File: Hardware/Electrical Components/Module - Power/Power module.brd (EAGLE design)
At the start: 140 x 70 mm, 97 parts

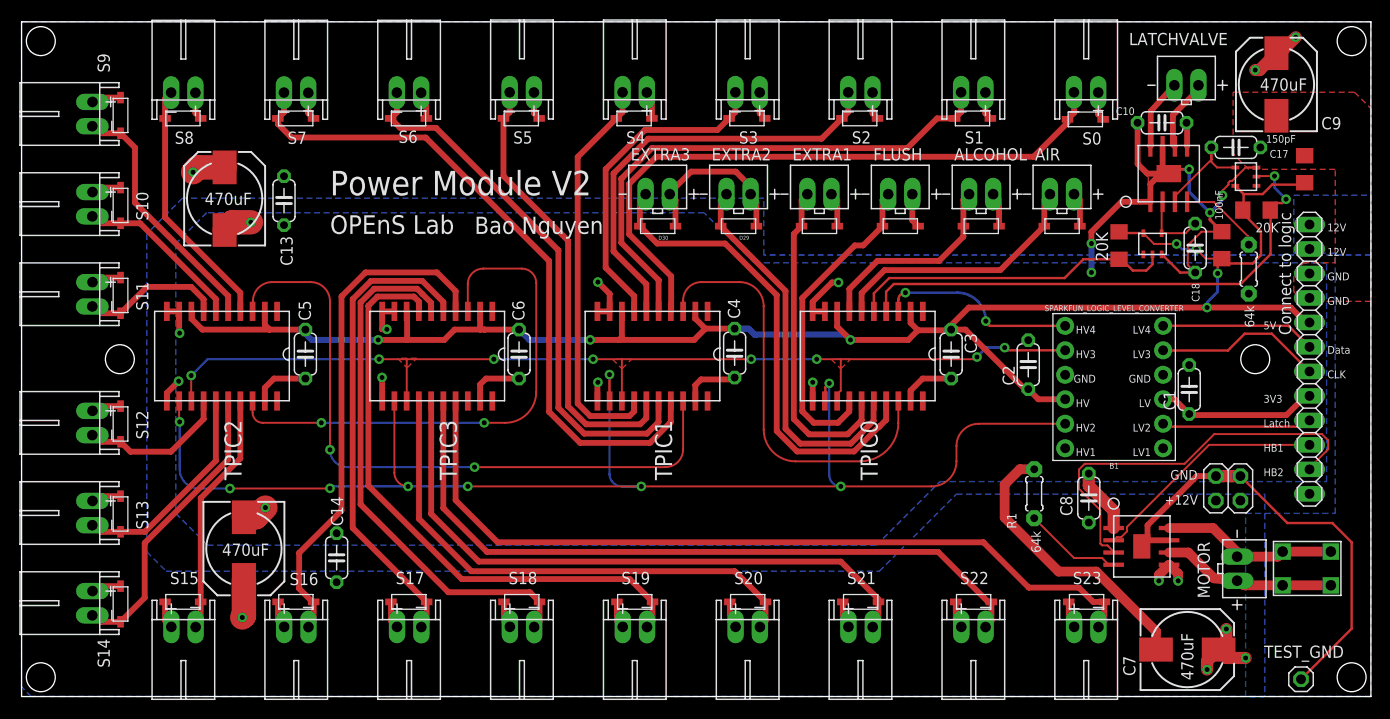
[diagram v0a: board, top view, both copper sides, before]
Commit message: Major fix for sensor module
O Power Module: Changes in footprint location of motor push-to-connect for mounting place. Move the 90-angle header further inside for better mechanical support
O Sensor Module: Rearrange 2.5mm headphone jack closer to the edge for proper mounting. The older version stops the male jack fully dock with the female casing thus fail to connect. Move the 90-angle header further inside for better mechanical support.
O MS5803-02BA: Change symbol, change SDA -> SDO. This label caused the PCB to stop working with all I2C devices. Sensor Module: Rewire to the write SDA, tested.
+ Add MS5803-02BA Datasheet
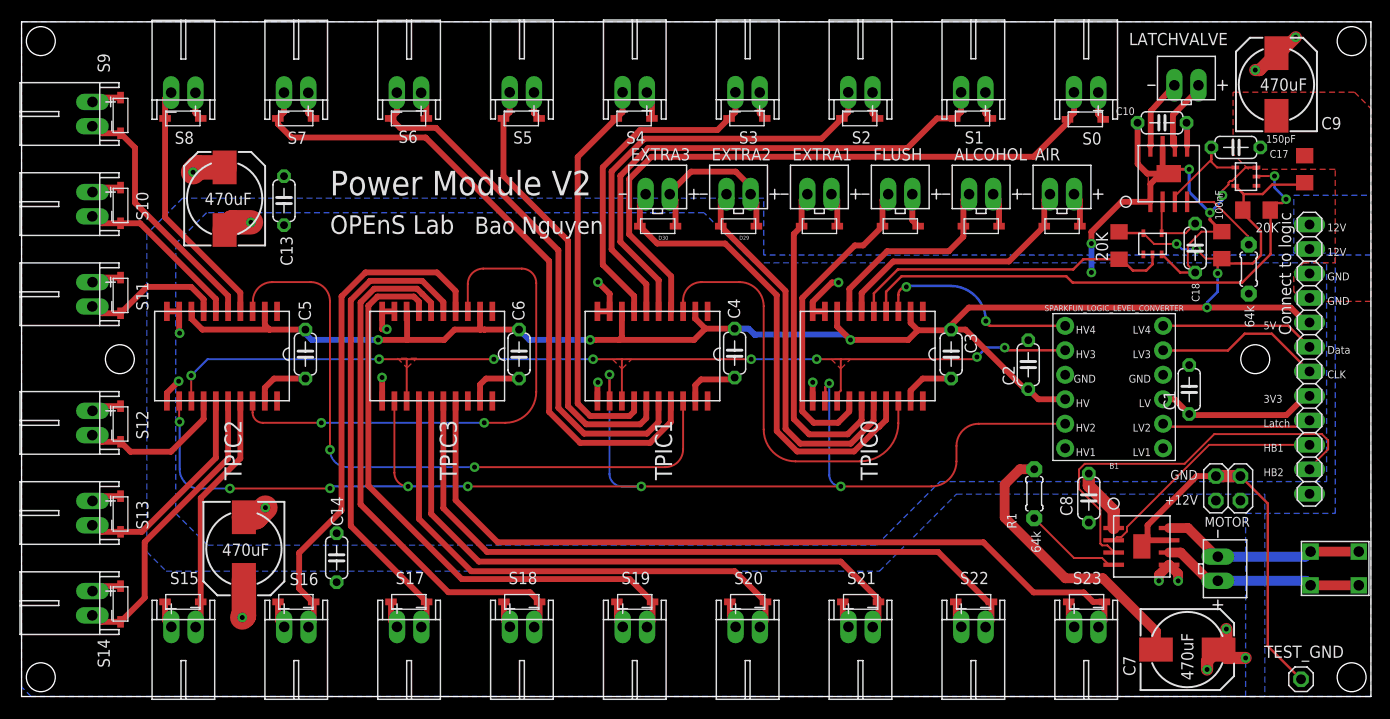
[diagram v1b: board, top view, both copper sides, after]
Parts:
- moved U$1 2.90 mm to (136.1, 13.3)
- moved MOTOR 2.00 mm to (124.1, 13.3)
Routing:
- net GND: track 195.0 -> 187.9 mm
- net MOTOR2: track 18.0 -> 21.1 mm
- net MOTOR1: track 18.5 -> 21.1 mm
- net T_DATA: track 20.2 -> 21.1 mm
- net S4: track 33.9 -> 34.5 mm
- net LATCHVALVE1: track 55.2 -> 55.7 mm
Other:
- board text added: "Designed at Oregon State University"
- board text removed: "Designed and Assembled in Oregon State University"

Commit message: Updates
Updated eDNA Eagle Library
Update OpenSPower7.2 BOM
Add OpenSPower 7.2 ReadMe
Add picture for FlowSensor
General clean up
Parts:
- removed C2: 100nF, adafruit:C050-024X044
- moved U$1 5.00 mm to (131.1, 13.3)
- moved AIR 4.00 mm to (103.9, 52.1)
- moved ALCOHOL 4.00 mm to (95.6, 52.1)
- moved C10 4.00 mm to (114.3, 59.5)
- moved C11 4.00 mm to (120.5, 46.8)
- moved C12 4.00 mm to (129.1, 54.7)
- moved C17 4.00 mm to (122.0, 57.0)
- moved C18 4.00 mm to (117.8, 46.5)
- moved C7 4.00 mm to (117.0, 4.87)
- moved C8 4.00 mm to (106.7, 20.6)
- moved D1 4.00 mm to (106.4, 59.9)
- moved D24 4.00 mm to (106.5, 9.82)
- moved D25 4.00 mm to (104.0, 48.8)
- moved D26 4.00 mm to (95.6, 48.8)
- moved D27 4.00 mm to (87.2, 48.8)
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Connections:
- net +5V: no longer C2.1
- net GND: no longer C2.2
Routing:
- net T_RCK: track 143.1 -> 135.2 mm, vias 9 -> 7
- net +5V: track 192.4 -> 184.6 mm
- net S3: track 45.2 -> 52.5 mm
- net S4: track 34.5 -> 41.6 mm
- net S24: track 84.8 -> 78.1 mm
- net S22: track 64.9 -> 58.2 mm
- net S23: track 74.9 -> 68.2 mm
- net S2: track 55.9 -> 62.3 mm
- net S21: track 54.6 -> 48.3 mm
- net TPIC0_6: track 40.2 -> 46.2 mm
- net LATCHVALVE2: track 34.0 -> 28.0 mm
- net ALCOHOL: track 21.1 -> 15.1 mm
- net TPIC0_7: track 50.4 -> 56.4 mm
- net AIR: track 27.3 -> 21.3 mm
- net LATCHVALVE1: track 55.7 -> 49.7 mm
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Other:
- board size 140 x 70 mm -> 136 x 70 mm
